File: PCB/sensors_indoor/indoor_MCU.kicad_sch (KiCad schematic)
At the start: 14 parts, among them J2 STDC14, SW1 SW_Push, U2 STM32WBA5MMG, U3 FM24CL16B

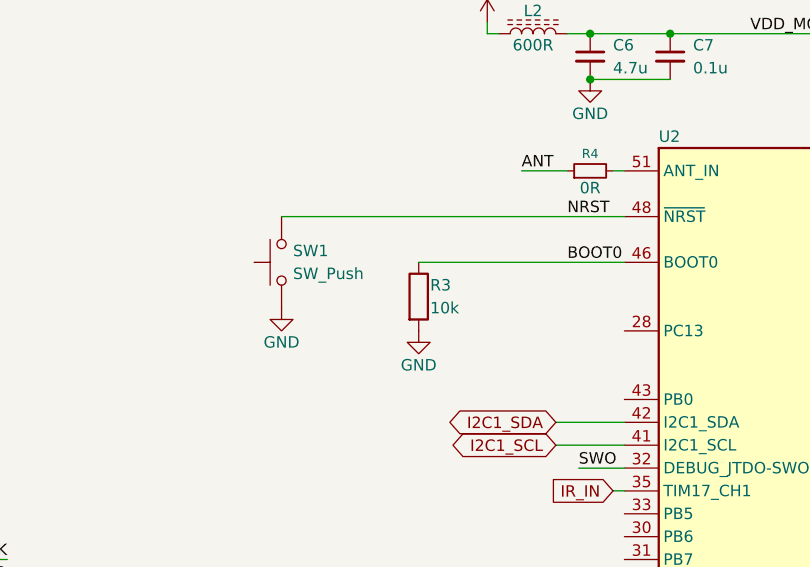
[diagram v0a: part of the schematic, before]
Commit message: Changed switch to SMD type
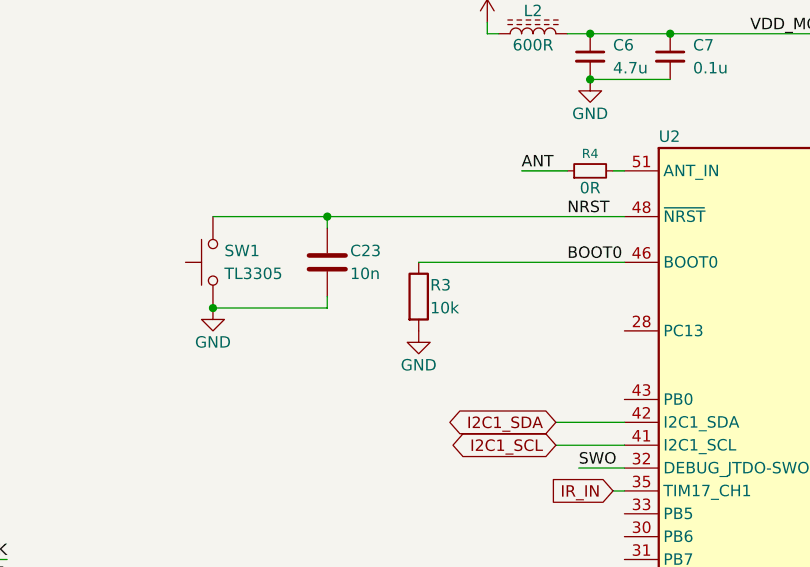
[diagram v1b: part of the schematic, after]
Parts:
- added C23: 10n, Capacitor_SMD:C_0402_1005Metric, symbol Device:C
- J2: footprint ZMPlib:SAMTEC_FTSH-107-01-L-DV-K-A -> DWlib:SAMTEC_FTSH-107-01-L-DV-K-A
- SW1: value SW_Push -> TL3305; footprint Button_Switch_THT:SW_PUSH_6mm -> DWlib:SW_Push_1P1T_NO_E-Switch_TL3305AFxxxQG; MPN (none) -> TL3305AF260QG; Mouser PN (none) -> 612-TL3305AF260QG
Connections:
- net GND: now also C23.2
- net NRST: now also C23.1
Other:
- moved on the sheet: SW1
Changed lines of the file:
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@@
+	)
+	(junction
+		(at 91.44 66.04)
+		(diameter 0)
+		(color 0 0 0 0)
 	)
 	(junction
@@
 	)
 	(junction
+		(at 78.74 76.2)
+		(diameter 0)
+		(color 0 0 0 0)
+	)
+	(junction
 		(at 35.56 129.54)
 		(diameter 0)
@@
 	(wire
 		(pts
+			(xy 91.44 66.04) (xy 124.46 66.04)
+		)
+		(stroke
+			(width 0)
+			(type default)
+		)
+	)
+	(wire
+		(pts
 			(xy 228.6 71.12) (xy 240.03 71.12)
 		)
@@
 	(wire
 		(pts
+			(xy 91.44 74.93) (xy 91.44 76.2)
+		)
+		(stroke
+			(width 0)
+			(type default)
+		)
+	)
+	(wire
+		(pts
 			(xy 173.99 86.36) (xy 172.72 86.36)
 		)
@@
 	(wire
 		(pts
+			(xy 91.44 66.04) (xy 91.44 67.31)
+		)
+		(stroke
+			(width 0)
+			(type default)
+		)
+	)
+	(wire
+		(pts
 			(xy 173.99 106.68) (xy 172.72 106.68)
 		)
@@
 	(wire
 		(pts
-			(xy 86.36 66.04) (xy 124.46 66.04)
+			(xy 91.44 76.2) (xy 78.74 76.2)
+		)
+		(stroke
+			(width 0)
+			(type default)
+		)
+	)
+	(wire
+		(pts
+			(xy 78.74 66.04) (xy 91.44 66.04)
 		)
 		(stroke
@@
 			)
 		)
-		(property "Footprint" "ZMPlib:SAMTEC_FTSH-107-01-L-DV-K-A"
+		(property "Footprint" "DWlib:SAMTEC_FTSH-107-01-L-DV-K-A"
 			(at 35.56 111.76 0)
 			(effects
@@
 	)
 	(symbol
+		(lib_id "Device:C")
+		(at 91.44 71.12 0)
+		(unit 1)
+		(exclude_from_sim no)
+		(in_bom yes)
+		(on_board yes)
+		(dnp no)
+		(property "Reference" "C23"
+			(at 93.98 69.85 0)
+			(effects
+				(font
+					(size 1.27 1.27)
+				)
+				(justify left)
+			)
+		)
+		(property "Value" "10n"
+			(at 93.98 72.39 0)
+			(effects
+				(font
+					(size 1.27 1.27)
+				)
+				(justify left)
+			)
+		)
+		(property "Footprint" "Capacitor_SMD:C_0402_1005Metric"
+			(at 92.4052 74.93 0)
+			(effects
+				(font
+					(size 1.27 1.27)
+				)
+				(hide yes)
+			)
+		)
+		(property "Datasheet" "~"
+			(at 91.44 71.12 0)
+			(effects
+				(font
+					(size 1.27 1.27)
+				)
+				(hide yes)
+			)
+		)
+		(property "Description" "Unpolarized capacitor"
+			(at 91.44 71.12 0)
+			(effects
+				(font
+					(size 1.27 1.27)
+				)
+				(hide yes)
+			)
+		)
+		(pin "1"
+		)
+		(pin "2"
+		)
+		(instances
+			(project "sensors_indoor"
+				(path "/09bb465b-75b9-463f-b128-e813d3269ff6/5392948c-5a35-4c1f-85ab-ec60577b6d09"
+					(reference "C23")
+					(unit 1)
+				)
+			)
+		)
+	)
+	(symbol
 		(lib_id "Device:R")
 		(at 247.65 66.04 0)
@@
 	(symbol
 		(lib_id "Switch:SW_Push")
-		(at 86.36 71.12 90)
+		(at 78.74 71.12 90)
 		(unit 1)
 		(exclude_from_sim no)
@@
 		(fields_autoplaced yes)
 		(property "Reference" "SW1"
-			(at 87.63 69.8499 90)
+			(at 80.01 69.8499 90)
 			(effects
 				(font
@@
 			)
 		)
-		(property "Value" "SW_Push"
-			(at 87.63 72.3899 90)
+		(property "Value" "TL3305"
+			(at 80.01 72.3899 90)
 			(effects
 				(font
@@
 			)
 		)
-		(property "Footprint" "Button_Switch_THT:SW_PUSH_6mm"
-			(at 81.28 71.12 0)
+		(property "Footprint" "DWlib:SW_Push_1P1T_NO_E-Switch_TL3305AFxxxQG"
+			(at 73.66 71.12 0)
 			(effects
 				(font
@@
 		)
 		(property "Datasheet" "~"
-			(at 81.28 71.12 0)
+			(at 73.66 71.12 0)
 			(effects
 				(font
@@
 		)
 		(property "Description" "Push button switch, generic, two pins"
-			(at 86.36 71.12 0)
+			(at 78.74 71.12 0)
+			(effects
+				(font
+					(size 1.27 1.27)
+				)
+				(hide yes)
+			)
+		)
+		(property "MPN" "TL3305AF260QG"
+			(at 78.74 71.12 90)
+			(effects
+				(font
+					(size 1.27 1.27)
+				)
+				(hide yes)
+			)
+		)
+		(property "Mouser PN" "612-TL3305AF260QG"
+			(at 78.74 71.12 90)
 			(effects
 				(font
@@
 	(symbol
 		(lib_id "power:GND")
-		(at 86.36 76.2 0)
+		(at 78.74 76.2 0)
 		(unit 1)
 		(exclude_from_sim no)
@@
 		(dnp no)
 		(property "Reference" "#PWR014"
-			(at 86.36 82.55 0)
+			(at 78.74 82.55 0)
 			(effects
 				(font
@@
 		)
 		(property "Value" "GND"
-			(at 86.36 80.01 0)
+			(at 78.74 80.01 0)
 			(effects
 				(font
@@
 		)
 		(property "Footprint" ""
-			(at 86.36 76.2 0)
+			(at 78.74 76.2 0)
 			(effects
 				(font
@@
 		)
 		(property "Datasheet" ""
-			(at 86.36 76.2 0)
+			(at 78.74 76.2 0)
 			(effects
 				(font
@@
 		)
 		(property "Description" "Power symbol creates a global label with name \"GND\" , ground"
-			(at 86.36 76.2 0)
-			(effects
-				(font
+			(at 78.74 76.2 0)
+			(effects
+				(font

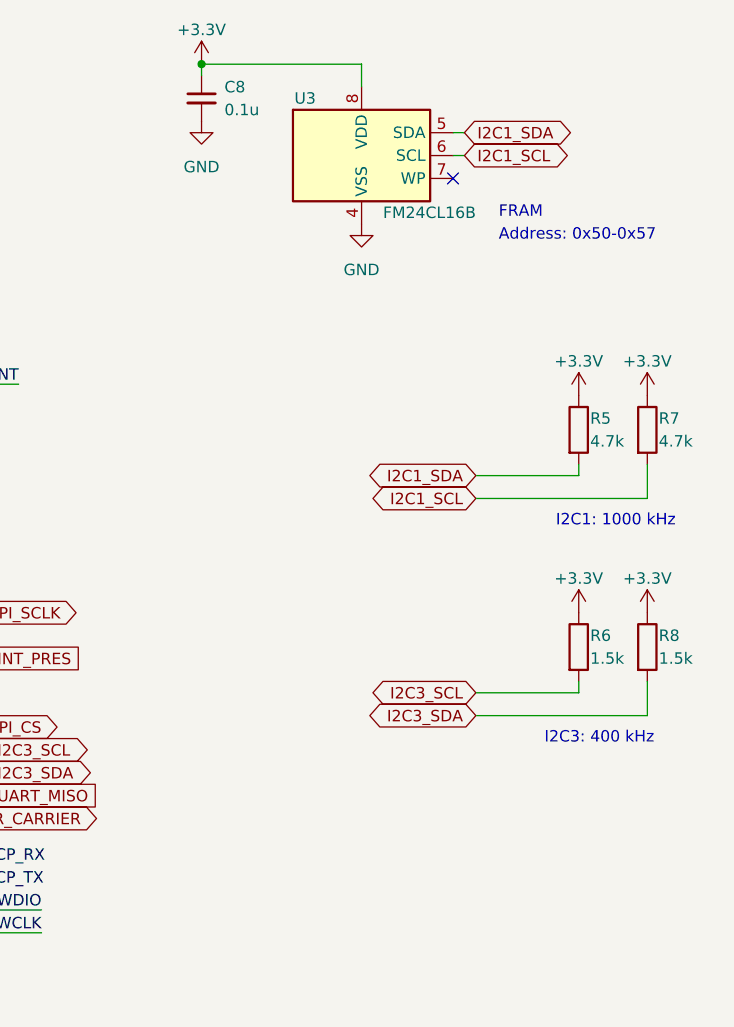
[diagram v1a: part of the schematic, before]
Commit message: Added UV sensor
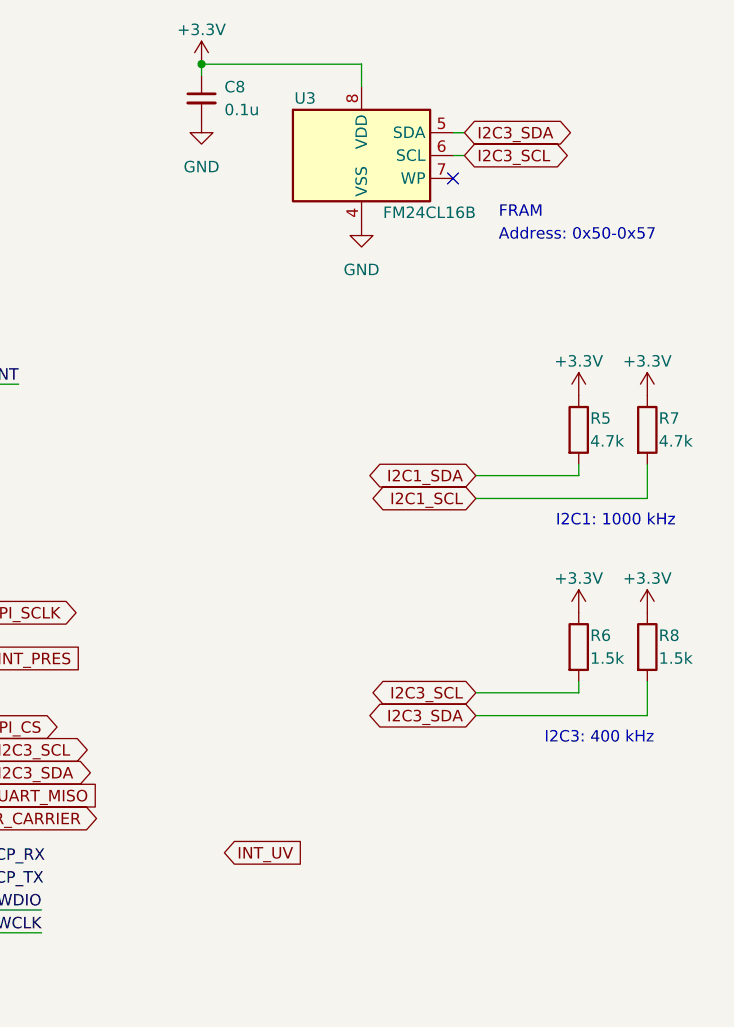
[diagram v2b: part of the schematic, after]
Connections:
- net I2C1_SCL: no longer U3.6 (SCL)
- net I2C1_SDA: no longer U3.5 (SDA)
- net I2C3_SCL: now also U3.6 (SCL)
- net I2C3_SDA: now also U3.5 (SDA)
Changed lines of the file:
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@@
+		)
+	)
+	(global_label "I2C3_SDA"
+		(shape bidirectional)
+		(at 227.33 33.02 0)
+		(fields_autoplaced yes)
+		(effects
+			(font
+				(size 1.27 1.27)
+			)
+			(justify left)
+		)
+		(property "Intersheetrefs" "${INTERSHEET_REFS}"
+			(at 239.1447 33.02 0)
+			(effects
+				(font
+					(size 1.27 1.27)
+				)
+				(justify left)
+			)
 		)
 	)
@@
 		)
 	)
-	(global_label "I2C1_SCL"
+	(global_label "I2C3_SCL"
 		(shape bidirectional)
 		(at 227.33 35.56 0)
@@
 		)
 	)
+	(global_label "INT_UV"
+		(shape input)
+		(at 200.66 113.03 0)
+		(fields_autoplaced yes)
+		(effects
+			(font
+				(size 1.27 1.27)
+			)
+			(justify left)
+		)
+		(property "Intersheetrefs" "${INTERSHEET_REFS}"
+			(at 209.9348 113.03 0)
+			(effects
+				(font
+					(size 1.27 1.27)
+				)
+				(justify left)
+			)
+		)
+	)
 	(global_label "I2C3_SDA"
 		(shape bidirectional)
@@
 			(effects
 				(font
-					(size 1.27 1.27)
-				)
-				(justify left)
-			)
-		)
-	)
-	(global_label "I2C1_SDA"
-		(shape bidirectional)
-		(at 227.33 33.02 0)
-		(fields_autoplaced yes)
-		(effects
-			(font
-				(size 1.27 1.27)
-			)
-			(justify left)
-		)
-		(property "Intersheetrefs" "${INTERSHEET_REFS}"
-			(at 239.1447 33.02 0)
-			(effects
-				(font

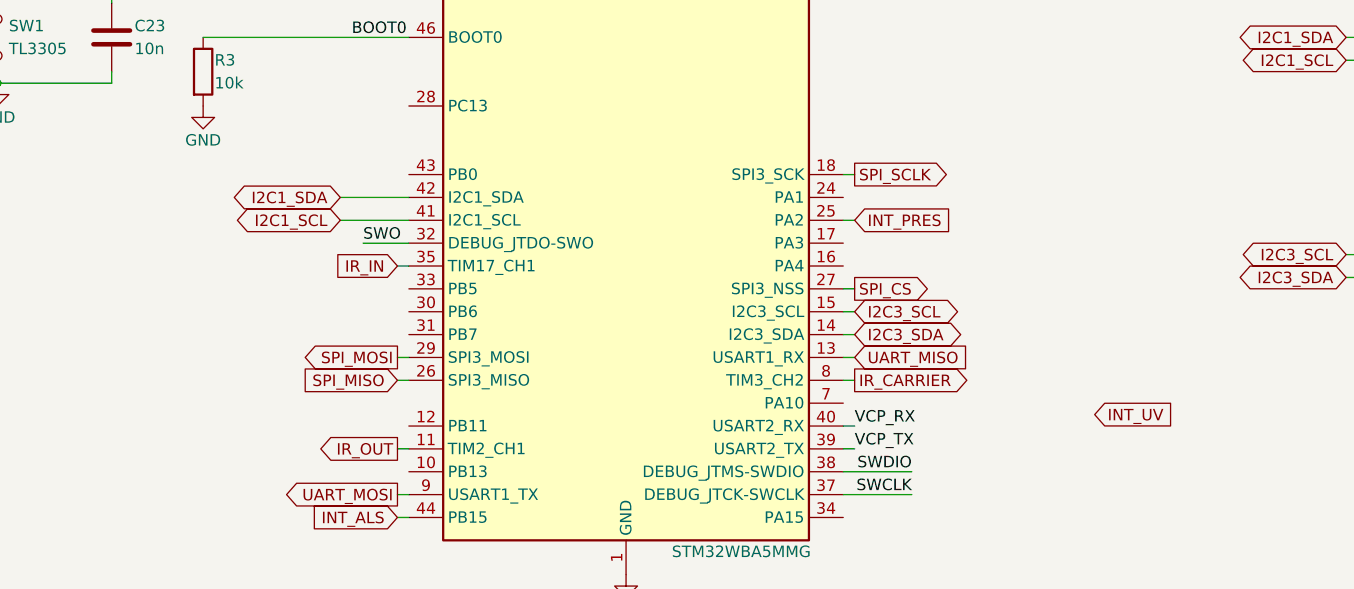
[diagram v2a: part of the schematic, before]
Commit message: Completed routing connections
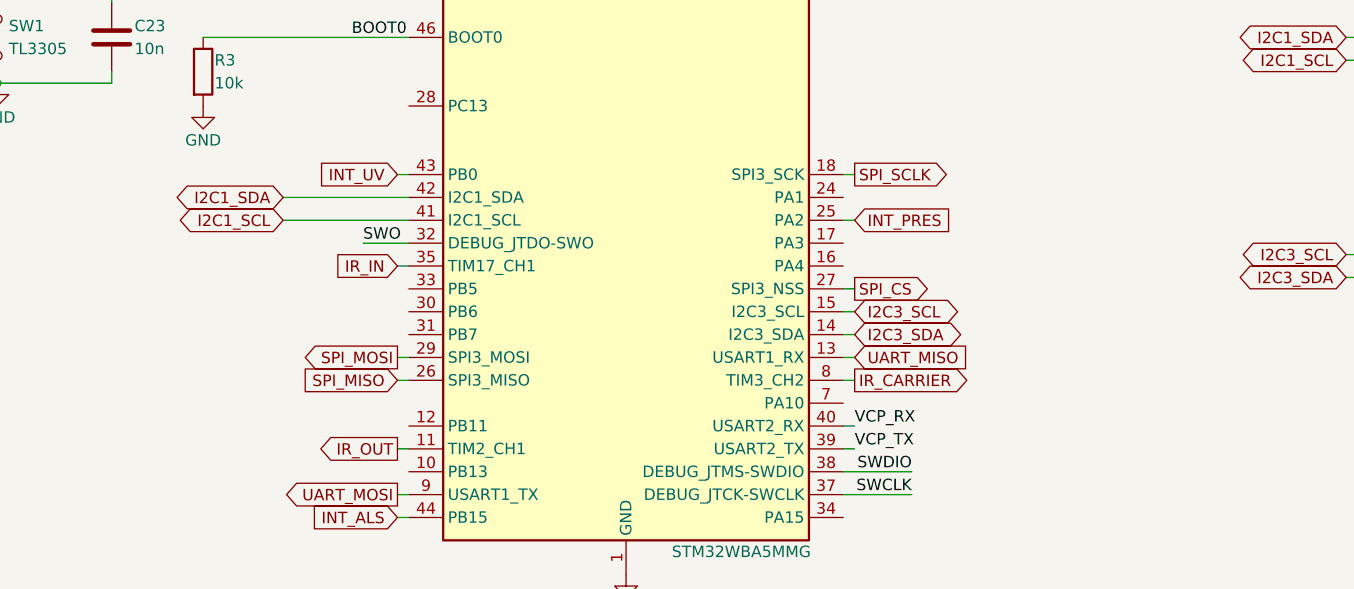
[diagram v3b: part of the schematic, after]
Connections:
- net INT_UV: now also U2.43 (PB0)
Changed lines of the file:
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@@
+	(wire
+		(pts
+			(xy 123.19 86.36) (xy 124.46 86.36)
+		)
+		(stroke
+			(width 0)
+			(type default)
+		)
+	)
 	(wire
 		(pts
@@
 	(wire
 		(pts
-			(xy 116.84 91.44) (xy 124.46 91.44)
+			(xy 110.49 91.44) (xy 124.46 91.44)
 		)
 		(stroke
@@
 	(wire
 		(pts
-			(xy 116.84 88.9) (xy 124.46 88.9)
+			(xy 110.49 88.9) (xy 124.46 88.9)
 		)
 		(stroke
@@
 	(global_label "INT_UV"
 		(shape input)
-		(at 200.66 113.03 0)
-		(fields_autoplaced yes)
-		(effects
-			(font
-				(size 1.27 1.27)
-			)
-			(justify left)
-		)
-		(property "Intersheetrefs" "${INTERSHEET_REFS}"
-			(at 209.9348 113.03 0)
-			(effects
-				(font
-					(size 1.27 1.27)
-				)
-				(justify left)
+		(at 123.19 86.36 180)
+		(fields_autoplaced yes)
+		(effects
+			(font
+				(size 1.27 1.27)
+			)
+			(justify right)
+		)
+		(property "Intersheetrefs" "${INTERSHEET_REFS}"
+			(at 113.9152 86.36 0)
+			(effects
+				(font
+					(size 1.27 1.27)
+				)
+				(justify right)
 			)
 		)
@@
 	(global_label "I2C1_SDA"
 		(shape bidirectional)
-		(at 116.84 88.9 180)
-		(fields_autoplaced yes)
-		(effects
-			(font
-				(size 1.27 1.27)
-			)
-			(justify right)
-		)
-		(property "Intersheetrefs" "${INTERSHEET_REFS}"
-			(at 105.0253 88.9 0)
+		(at 110.49 88.9 180)
+		(fields_autoplaced yes)
+		(effects
+			(font
+				(size 1.27 1.27)
+			)
+			(justify right)
+		)
+		(property "Intersheetrefs" "${INTERSHEET_REFS}"
+			(at 98.6753 88.9 0)
 			(effects
 				(font
@@
 	(global_label "I2C1_SCL"
 		(shape bidirectional)
-		(at 116.84 91.44 180)
-		(fields_autoplaced yes)
-		(effects
-			(font
-				(size 1.27 1.27)
-			)
-			(justify right)
-		)
-		(property "Intersheetrefs" "${INTERSHEET_REFS}"
-			(at 105.0858 91.44 0)
-			(effects
-				(font
+		(at 110.49 91.44 180)
+		(fields_autoplaced yes)
+		(effects
+			(font
+				(size 1.27 1.27)
+			)
+			(justify right)
+		)
+		(property "Intersheetrefs" "${INTERSHEET_REFS}"
+			(at 98.7358 91.44 0)
+			(effects
+				(font
